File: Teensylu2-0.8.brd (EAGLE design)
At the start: 101.6 x 76.2 mm, 113 parts, among them IC1 AT90USB1286, J1 MICROSD, J2 USB-MICRO-PTH, J3 4P-TERM-BLOCK284391-4, J4 39-29-3066, J5 4P-TERM-BLOCK282834-4, J6 2x7, J7 4P-TERM-BLOCK284391-4, J8 4P-TERM-BLOCK282834-4, P1 POLOLU-X, P2 POLOLU-Y, P3 POLOLU-Z, P4 POLOLU-E, P5 POLOLU-E, Q1 PMV45EN, Q2 PSMN1R2-30YLCPOWERPACK-S08, Q3 PSMN1R2-30YLCPOWERPACK-S08, Q4 PSMN1R2-30YLCPOWERPACK-S08, U1 LMR16006X, U2 PRTR5V0U4DSOT23-6, U3 AP7313SOT23C, U4 TXB0104TSSOP14, X1 16MHZ

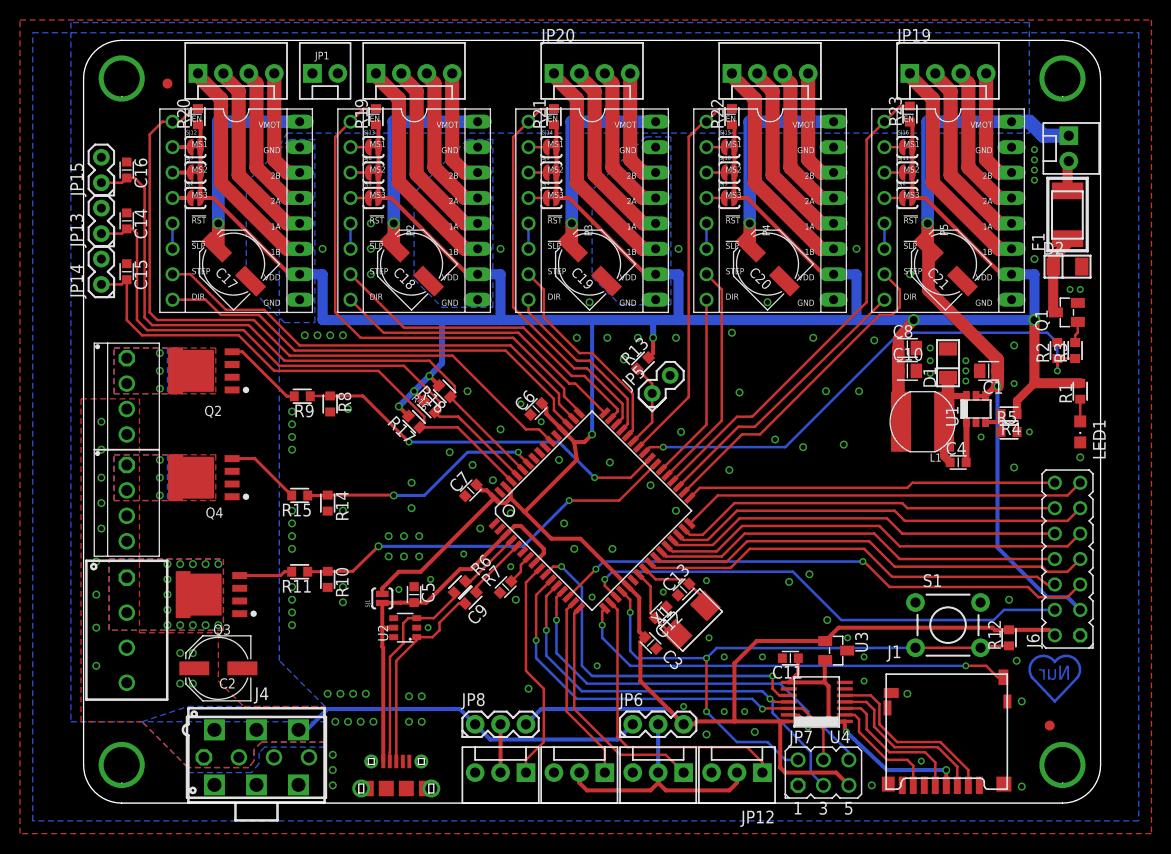
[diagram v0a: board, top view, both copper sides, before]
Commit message: Beta Release
This is a BETA release. The design is pending review.
Changes:
Added more via's to the Mosfets. Silkscreen is complete. Reset button
changed to SMD. Moved endstop voltage selector. Capacitors are now all
SMD. Teensylu lib should contain all of the components.
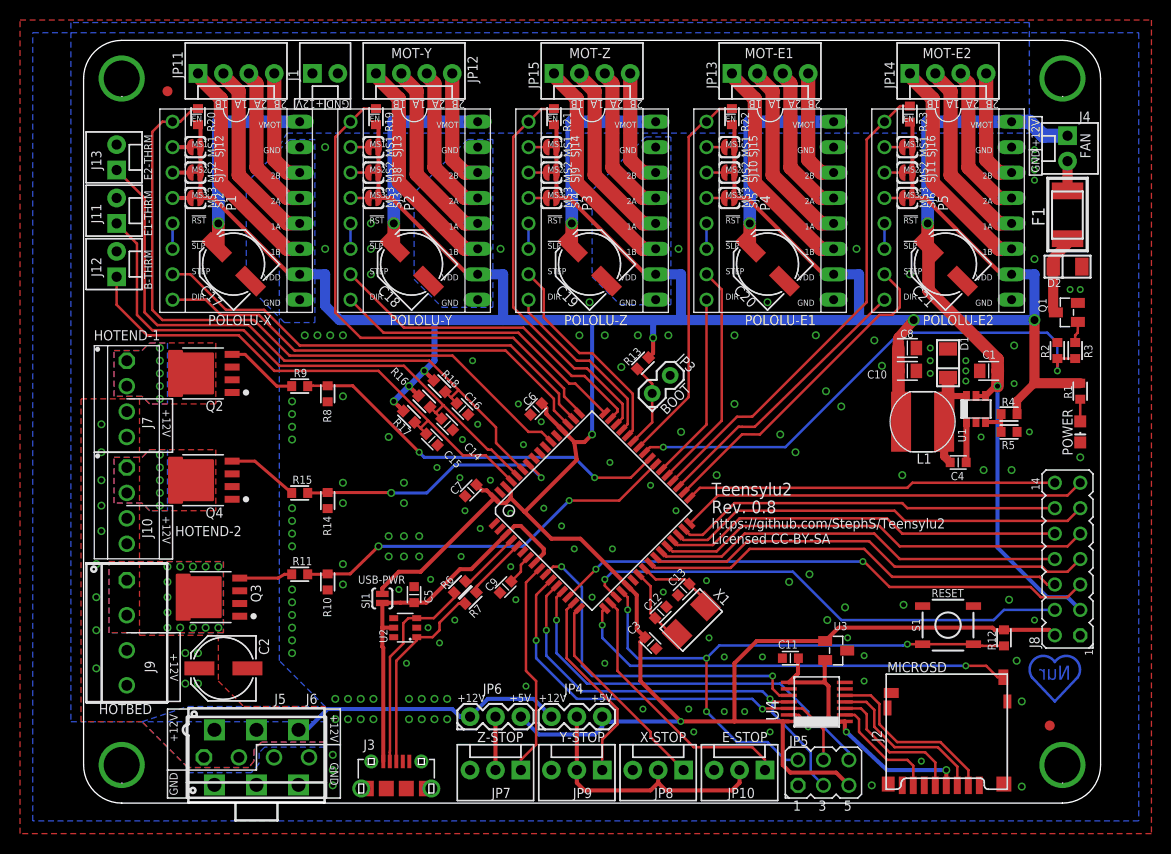
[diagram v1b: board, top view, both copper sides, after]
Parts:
- removed JP16: MOT-X, teensylu:MOLEX-1X4
- removed JP17: MOT-Y, teensylu:MOLEX-1X4
- removed JP18, JP19: MOT-E, teensylu:MOLEX-1X4
- removed JP20: MOT-Z, teensylu:MOLEX-1X4
- added J10: HOTEND-2, teensylu:282834-4
- added J11: E1-THRM, teensylu:MOLEX-1X2
- added J12: B-THRM, teensylu:MOLEX-1X2
- added J13: E2-THRM, teensylu:MOLEX-1X2
- added J9: HOTBED, teensylu:284391-4
- C17, C18, C19, C2, C20, C21: device rcl:PANASONIC_D -> teensylu:PANASONIC_D
- J1: value MICROSD -> 12VPWR; device teensylu:AMPHENOL-MICROSD -> teensylu:MOLEX-1X2
- J2: value USB-MICRO-PTH -> MICROSD; device teensylu:USB-MICROB-PTH -> teensylu:AMPHENOL-MICROSD
- J3: value 4P-TERM-BLOCK284391-4 -> USB-MICRO-PTH; device teensylu:284391-4 -> teensylu:USB-MICROB-PTH
- J4: value 39-29-3066 -> FAN; device teensylu:39-29-3066 -> teensylu:MOLEX-1X2
- J5: value 4P-TERM-BLOCK282834-4 -> 4P-TERM-BLOCK284391-4; device teensylu:282834-4 -> teensylu:284391-4
- J6: value 2x7 -> 39-29-3066; device teensylu:JP7Q -> teensylu:39-29-3066
- J7: value 4P-TERM-BLOCK284391-4 -> HOTEND-1; device teensylu:284391-4 -> teensylu:282834-4
- J8: value 4P-TERM-BLOCK282834-4 -> 2x7; device teensylu:282834-4 -> teensylu:JP7Q
- JP1: value 12VPWR -> FIDUCIAL1X2.5; device teensylu:MOLEX-1X2 -> SparkFun:FIDUCIAL-1X2.5
- JP10: value X-STOP -> E-STOP
- JP11: value Y-STOP -> MOT-X; device teensylu:MOLEX-1X3 -> teensylu:MOLEX-1X4
- JP12: value E-STOP -> MOT-Y; device teensylu:MOLEX-1X3 -> teensylu:MOLEX-1X4
- JP13: value (none) -> MOT-E1; device teensylu:1X02 -> teensylu:MOLEX-1X4
- JP14: value (none) -> MOT-E2; device teensylu:1X02 -> teensylu:MOLEX-1X4
- JP15: value (none) -> MOT-Z; device teensylu:1X02 -> teensylu:MOLEX-1X4
- JP2: value FAN -> FIDUCIAL1X2.5; device teensylu:MOLEX-1X2 -> SparkFun:FIDUCIAL-1X2.5
- JP3: value FIDUCIAL1X2.5 -> BOOT; device SparkFun:FIDUCIAL-1X2.5 -> teensylu:1X02
- JP4: value FIDUCIAL1X2.5 -> X-STOP-VOLTAGE; device SparkFun:FIDUCIAL-1X2.5 -> teensylu:1X03
- JP5: value BOOT -> ISP; device teensylu:1X02 -> teensylu:ISP
- JP6: value JUMPER-3PTH -> Z-STOP-VOLTAGE
- JP7: value (none) -> Z-STOP; device teensylu:ISP -> teensylu:MOLEX-1X3
- JP8: value JUMPER-3PTH -> X-STOP; device teensylu:1X03 -> teensylu:MOLEX-1X3
- JP9: value Z-STOP -> Y-STOP
- LED1: value (none) -> POWER; device led:CHIPLED_0805 -> teensylu:CHIPLED_0805
- P4: value POLOLU-E -> POLOLU-E1
- P5: value POLOLU-E -> POLOLU-E2
- Q2, Q3, Q4: value PSMN1R2-30YLCPOWERPACK-S08 -> PSMN1R2-30YLC
- S1: device SparkFun:TACTILE-PTH -> teensylu:TACTILE_SWITCH_SMD
- SJ1: value SOLDERJUMPERNO -> USB-PWR
- SJ10, SJ11, SJ7, SJ8, SJ9: value SOLDERJUMPER-NCSJ-TRACE -> MS2
- SJ12, SJ13, SJ14, SJ15, SJ16: value SOLDERJUMPER-NCSJ-TRACE -> MS1
- SJ2, SJ3, SJ4, SJ5, SJ6: value SOLDERJUMPER-NCSJ-TRACE -> MS3
- moved J4 102.1 mm to (98.3, 66.7), turned to 270 degrees
- moved J8 94.1 mm to (98.3, 24.4), turned to 90 degrees
- moved J1 90.7 mm to (22.9, 72.9)
- moved JP14 83.5 mm to (82.5, 72.9), turned to 0 degrees
- moved J6 83.4 mm to (17.3, 4.57), turned to 180 degrees
- moved JP11 80.8 mm to (11.4, 72.9), turned to 0 degrees
- moved JP12 79.8 mm to (29.2, 72.9), turned to 0 degrees
- moved JP13 65.0 mm to (64.8, 72.9), turned to 0 degrees
- moved JP2 59.0 mm to (96.5, 7.75), turned to 0 degrees
- moved JP3 57.5 mm to (56.8, 40.9), turned to 45 degrees
- moved J2 55.0 mm to (85.9, 7.62)
- moved JP4 49.8 mm to (46.7, 8.64)
- moved JP15 46.5 mm to (47.0, 72.9), turned to 0 degrees
- moved JP5 41.6 mm to (73.9, 3.05), turned to 0 degrees
- moved C16 41.2 mm to (37.8, 39.4), turned to 135 degrees
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- renumbered IC1 to U5
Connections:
- removed net E-MOT-1A1: JP19.2, P5.1A
- removed net E-MOT-1B1: JP19.1, P5.1B
- removed net E-MOT-2A1: JP19.3, P5.2A
- removed net E-MOT-2B1: JP19.4, P5.2B
- new net E2-MOT-1A: JP14.2, P5.1A
- new net E2-MOT-1B: JP14.1, P5.1B
- new net E2-MOT-2A: JP14.3, P5.2A
- new net E2-MOT-2B: JP14.4, P5.2B
- net !RESET: now also JP5.2; no longer JP7.2
- net +3V3: now also J2.4; no longer J1.4
- net 12V: now also J1.1, J10.3, J10.4, J5.1, J5.2, J6.1, J6.2, J9.3, J9.4, JP4.1; no longer J3.1, J3.2, J4.2, J4.3, J5.3, J5.4, J8.4, JP1.1, JP2.1, JP8.1
- net 5V: now also J8.2, JP4.3, JP5.5; no longer J6.2, JP7.5, JP8.3
- net ALE: now also JP3.1; no longer JP5.1
- net B-THERM: now also J12.1; no longer JP14.1
- net E-MOT-1A: now also JP13.2; no longer JP18.2
- net E-MOT-1B: now also JP13.1; no longer JP18.1
- net E-MOT-2A: now also JP13.3; no longer JP18.3
- net E-MOT-2B: now also JP13.4; no longer JP18.4
- net E-STOP: now also JP10.1; no longer JP12.1
- net E1-THERM: now also J11.1; no longer JP13.1
- net E2-THERM: now also J13.1; no longer JP15.1
- net ENDSTOP+V: now also JP4.2, JP8.2, JP9.2; no longer JP11.2, JP12.2, JP6.2
- net GND: now also J1.2, J11.2, J12.2, J13.2, J2.6, J2.C1, J2.C2, J2.C3, J2.C4, J2.CD1, J3.GND, J3.GND1, J3.GND2, J3.GND3, J3.GND4, J3.GND5, J3.GND6, J3.GND7, J3.GND8, J5.3, J5.4, J6.4, J6.5, J6.6, J8.1, JP3.2, JP5.1, JP7.3, JP8.3; no longer J1.6, J1.C1, J1.C2, J1.C3, J1.C4, J1.CD1, J2.GND, J2.GND1, J2.GND2, J2.GND3, J2.GND4, J2.GND5, J2.GND6, J2.GND7, J2.GND8, J3.3, J3.4, J4.4, J4.5, J4.6, J6.1, JP1.2, JP11.3, JP12.3, JP13.2, JP14.2, JP15.2, JP5.2, JP7.1
- net HOTBED-GND: now also J9.1, J9.2; no longer J7.1, J7.2
- net HOTEND-GND: now also J7.1, J7.2; no longer J5.1, J5.2
- net HOTEND-GND1: now also J10.1, J10.2; no longer J8.1, J8.2
- net MISO: now also JP5.6; no longer JP7.6
- net MOSI: now also JP5.3; no longer JP7.3
- net N$5: now also J4.2; no longer JP2.2
- net PB4: now also J8.5; no longer J6.5
- net PD0-SCL: now also J8.6; no longer J6.6
- net PD1-SDA: now also J8.7; no longer J6.7
- net PD2-RX1: now also J8.8; no longer J6.8
- net PD3-TX1: now also J8.9; no longer J6.9
- net PD4: now also J8.10; no longer J6.10
- net PD5: now also J8.11; no longer J6.11
- net PD6: now also J8.12; no longer J6.12
- net PD7: now also J8.13; no longer J6.13
- net PE0: now also J8.14; no longer J6.14
- net PE5: now also J8.4; no longer J6.4
- net SCLK: now also JP5.4; no longer JP7.4
- net SDCD: now also J2.CD2; no longer J1.CD2
- net SDCLK: now also J2.5; no longer J1.5
- net SDCSH: now also J2.2; no longer J1.2
- net SDDI: now also J2.3; no longer J1.3
- net SDDO: now also J2.7; no longer J1.7
- net USB_DN: now also J3.D-; no longer J2.D-
- net USB_DP: now also J3.D+; no longer J2.D+
- net VBUS: now also J3.VBUS; no longer J2.VBUS
- net X-MOT-1A: now also JP11.2; no longer JP16.2
- net X-MOT-1B: now also JP11.1; no longer JP16.1
- net X-MOT-2A: now also JP11.3; no longer JP16.3
- net X-MOT-2B: now also JP11.4; no longer JP16.4
- net X-STOP: now also JP8.1; no longer JP10.1
- net Y-MOT-1A: now also JP12.2; no longer JP17.2
- net Y-MOT-1B: now also JP12.1; no longer JP17.1
- net Y-MOT-2A: now also JP12.3; no longer JP17.3
- net Y-MOT-2B: now also JP12.4; no longer JP17.4
- net Y-STOP: now also JP9.1; no longer JP11.1
- net Z-MOT-1A: now also JP15.2; no longer JP20.2
- net Z-MOT-1B: now also JP15.1; no longer JP20.1
- net Z-MOT-2A: now also JP15.3; no longer JP20.3
- net Z-MOT-2B: now also JP15.4; no longer JP20.4
- net Z-STOP: now also JP7.1; no longer JP9.1
- net Z-STOP-SUPPLY: now also JP6.2, JP7.2; no longer JP8.2, JP9.2
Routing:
- net E2-MOT-1B: track 0.00 -> 22.5 mm
- net E-MOT-1B1: track 22.5 -> 0.00 mm
- net E2-MOT-1A: track 0.00 -> 18.9 mm
- net E-MOT-1A1: track 18.9 -> 0.00 mm
- net E2-MOT-2A: track 0.00 -> 15.3 mm
- net E-MOT-2A1: track 15.3 -> 0.00 mm
- net E2-MOT-2B: track 0.00 -> 11.7 mm
- net E-MOT-2B1: track 11.7 -> 0.00 mm
- net 12V: track 193.2 -> 184.8 mm
- net E-STOP: track 30.3 -> 26.5 mm
- net X-STOP: track 23.8 -> 20.9 mm
- net !HOTEND-2: track 24.4 -> 26.9 mm
- net ENDSTOP+V: track 24.9 -> 26.7 mm
- net E1-THERM: track 58.2 -> 57.3 mm
- net Y-STOP: track 18.8 -> 19.7 mm
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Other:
- board text added: "+12V"
- board text added: "+5V"
- board text added: "1"
- board text added: "14"
- board text added: "2B 2A 1A 1B"
- board text added: "GND"
- board text added: "Licensed CC-BY-SA"
- board text added: "Rev. 0.8"
- board text added: "Teensylu2"
- board text added: "https://github.com/StephS/Teensylu2"

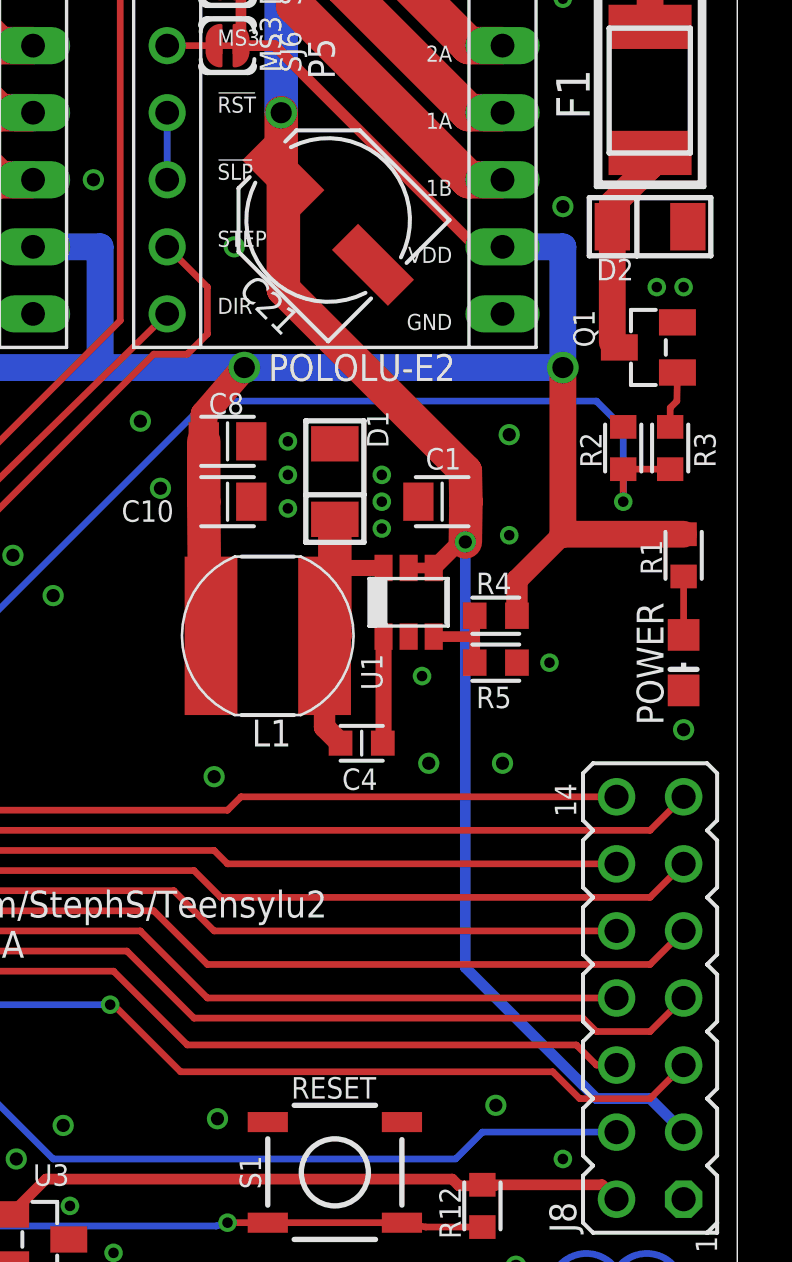
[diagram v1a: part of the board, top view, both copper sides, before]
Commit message: Updated BOM
Added a BOM, changed C1 to 1206 package.
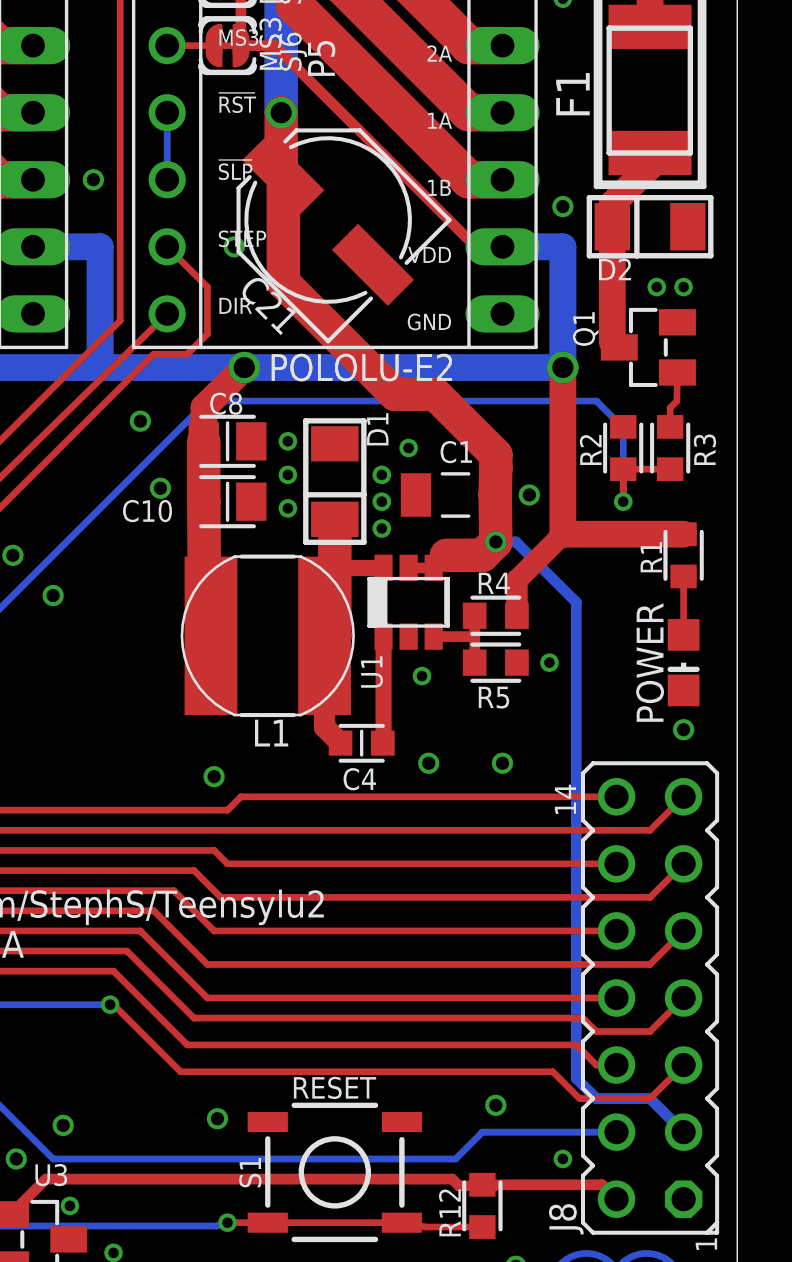
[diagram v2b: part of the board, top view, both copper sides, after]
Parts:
- C1: device teensylu:CAPC2012X145AN -> teensylu:CAPC3215X168N
- C4: value 100nF -> 0.1uF
- moved C1 0.57 mm to (90.9, 43.4)
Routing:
- net 12V: track 184.8 -> 187.3 mm
